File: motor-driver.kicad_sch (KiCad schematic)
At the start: 20 parts, among them J2 SIGNAL, J3 PWR, J4 RTMI

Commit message: Finish draft routing,
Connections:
- net +3.3V: no longer J2.1 (Pin_1)
- net +5V: now also J2.1 (Pin_1); no longer J2.2 (Pin_2)
- no-connect marks 3 -> 4
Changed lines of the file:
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@@
   (junction (at 64.77 151.13) (diameter 0) (color 0 0 0 0)
   )
-  (junction (at 127 127) (diameter 0) (color 0 0 0 0)
-  )
   (junction (at 142.24 149.86) (diameter 0) (color 0 0 0 0)
   )
@@
   )
   (no_connect (at 157.48 92.71))
+  (no_connect (at 140.97 127))
   (no_connect (at 170.18 100.33))
   (no_connect (at 157.48 118.11))
@@
     (stroke (width 0) (type default))
   )
-  (wire (pts (xy 128.27 127) (xy 127 127))
-    (stroke (width 0) (type default))
-  )
   (wire (pts (xy 140.97 142.24) (xy 153.67 142.24))
     (stroke (width 0) (type default))
@@
     (stroke (width 0) (type default))
   )
+  (wire (pts (xy 127 129.54) (xy 128.27 129.54))
+    (stroke (width 0) (type default))
+  )
   (wire (pts (xy 116.84 143.51) (xy 107.95 143.51))
     (stroke (width 0) (type default))
@@
     (stroke (width 0) (type default))
   )
-  (wire (pts (xy 140.97 127) (xy 142.24 127))
-    (stroke (width 0) (type default))
-  )
   (wire (pts (xy 20.32 55.88) (xy 33.02 55.88))
     (stroke (width 0) (type default))
@@
     (stroke (width 0) (type default))
   )
-  (wire (pts (xy 127 129.54) (xy 127 127))
-    (stroke (width 0) (type default))
-  )
   (wire (pts (xy 77.47 73.66) (xy 93.98 73.66))
     (stroke (width 0) (type default))
   )
-  (wire (pts (xy 128.27 129.54) (xy 127 129.54))
-    (stroke (width 0) (type default))
-  )
   (wire (pts (xy 77.47 55.88) (xy 90.17 55.88))
     (stroke (width 0) (type default))
@@
     (stroke (width 0) (type default))
   )
+  (wire (pts (xy 127 127) (xy 128.27 127))
+    (stroke (width 0) (type default))
+  )
   (wire (pts (xy 165.1 147.32) (xy 176.53 147.32))
     (stroke (width 0) (type default))
@@
     (stroke (width 0) (type default))
   )
-  (wire (pts (xy 127 125.73) (xy 127 127))
-    (stroke (width 0) (type default))
-  )
   (wire (pts (xy 20.32 22.86) (xy 33.02 22.86))
     (stroke (width 0) (type default))
@@
   )
   (wire (pts (xy 118.11 151.13) (xy 107.95 151.13))
-    (stroke (width 0) (type default))
-  )
-  (wire (pts (xy 142.24 127) (xy 142.24 125.73))
     (stroke (width 0) (type default))
   )
@@
     )
   )
+  (symbol (lib_id "power:+5V") (at 127 127 90) (unit 1)
+    (in_bom yes) (on_board yes) (dnp no)
+    (property "Reference" "#PWR04" (at 130.81 127 0)
+      (effects (font (size 1.27 1.27)) hide)
+    )
+    (property "Value" "+5V" (at 124.46 127 90)
+      (effects (font (size 1.27 1.27)) (justify left))
+    )
+    (property "Footprint" "" (at 127 127 0)
+      (effects (font (size 1.27 1.27)) hide)
+    )
+    (property "Datasheet" "" (at 127 127 0)
+      (effects (font (size 1.27 1.27)) hide)
+    )
+    (pin "1")
+    (instances
+      (project "motor-driver"
+        (path "/314549f2-cc46-4559-991a-ae9411f3d209/25794513-4b05-4cf2-b97c-a9dcfa280e83"
+          (reference "#PWR04") (unit 1)
+        )
+        (path "/314549f2-cc46-4559-991a-ae9411f3d209"
+          (reference "#PWR069") (unit 1)
+        )
+      )
+    )
+  )
   (symbol (lib_id "Device:R_Small_US") (at 105.41 132.08 90) (unit 1)
     (in_bom yes) (on_board yes) (dnp no)
@@
         (path "/314549f2-cc46-4559-991a-ae9411f3d209"
           (reference "C41") (unit 1)
-        )
-      )
-    )
-  )
-  (symbol (lib_id "power:+3.3V") (at 127 125.73 0) (unit 1)
-    (in_bom yes) (on_board yes) (dnp no)
-    (property "Reference" "#PWR054" (at 127 129.54 0)
-      (effects (font (size 1.27 1.27)) hide)
-    )
-    (property "Value" "+3.3V" (at 124.46 121.92 0)
-      (effects (font (size 1.27 1.27)) (justify left))
-    )
-    (property "Footprint" "" (at 127 125.73 0)
-      (effects (font (size 1.27 1.27)) hide)
-    )
-    (property "Datasheet" "" (at 127 125.73 0)
-      (effects (font (size 1.27 1.27)) hide)
-    )
-    (pin "1")
-    (instances
-      (project "motor-driver"
-        (path "/314549f2-cc46-4559-991a-ae9411f3d209/25794513-4b05-4cf2-b97c-a9dcfa280e83"
-          (reference "#PWR054") (unit 1)
-        )
-        (path "/314549f2-cc46-4559-991a-ae9411f3d209"
-          (reference "#PWR071") (unit 1)
         )
       )
@@
     )
   )
-  (symbol (lib_id "power:+5V") (at 142.24 125.73 0) (unit 1)
-    (in_bom yes) (on_board yes) (dnp no)
-    (property "Reference" "#PWR04" (at 142.24 129.54 0)
-      (effects (font (size 1.27 1.27)) hide)
-    )
-    (property "Value" "+5V" (at 139.7 121.92 0)
-      (effects (font (size 1.27 1.27)) (justify left))
-    )
-    (property "Footprint" "" (at 142.24 125.73 0)
-      (effects (font (size 1.27 1.27)) hide)
-    )
-    (property "Datasheet" "" (at 142.24 125.73 0)
-      (effects (font (size 1.27 1.27)) hide)
-    )
-    (pin "1")
-    (instances
-      (project "motor-driver"
-        (path "/314549f2-cc46-4559-991a-ae9411f3d209/25794513-4b05-4cf2-b97c-a9dcfa280e83"
-          (reference "#PWR04") (unit 1)
-        )
-        (path "/314549f2-cc46-4559-991a-ae9411f3d209"
-          (reference "#PWR069") (unit 1)
-        )
-      )
-    )
-  )
   (symbol (lib_id "power:+24V") (at 175.26 127 90) (unit 1)
     (in_bom yes) (on_board yes) (dnp no)
@@
         )
       )
+    )
+  )
+  (symbol (lib_id "power:+3.3V") (at 127 129.54 90) (unit 1)
+    (in_bom yes) (on_board yes) (dnp no)
+    (property "Reference" "#PWR054" (at 130.81 129.54 0)
+      (effects (font (size 1.27 1.27)) hide)
+    )
+    (property "Value" "+3.3V" (at 124.46 129.54 90)
+      (effects (font (size 1.27 1.27)) (justify left))
+    )
+    (property "Footprint" "" (at 127 129.54 0)
+      (effects (font (size 1.27 1.27)) hide)
+    )
+    (property "Datasheet" "" (at 127 129.54 0)
+      (effects (font (size 1.27 1.27)) hide)
+    )
+    (pin "1")
+    (instances
+      (project "motor-driver"
+        (path "/314549f2-cc46-4559-991a-ae9411f3d209/25794513-4b05-4cf2-b97c-a9dcfa280e83"
+          (reference "#PWR054") (unit 1)
+        )
+        (path "/314549f2-cc46-4559-991a-ae9411f3d209"
+          (reference "#PWR071") (unit 1)
+        )
+      )

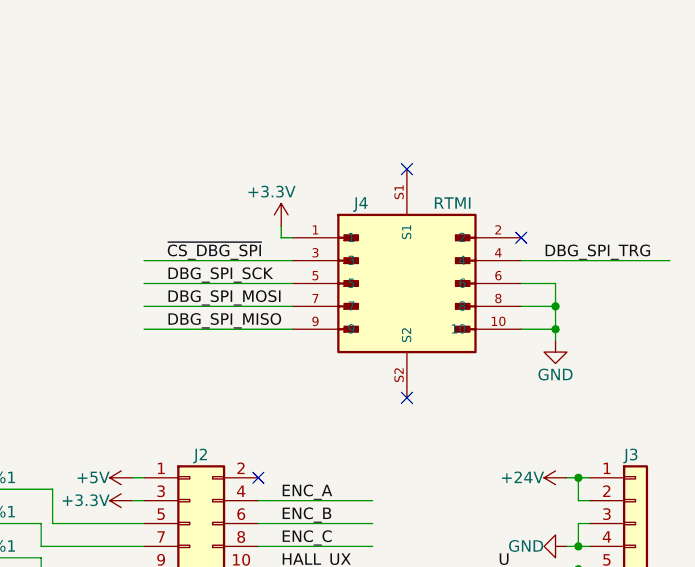
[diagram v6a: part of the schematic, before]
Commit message: Cleanup part properties.
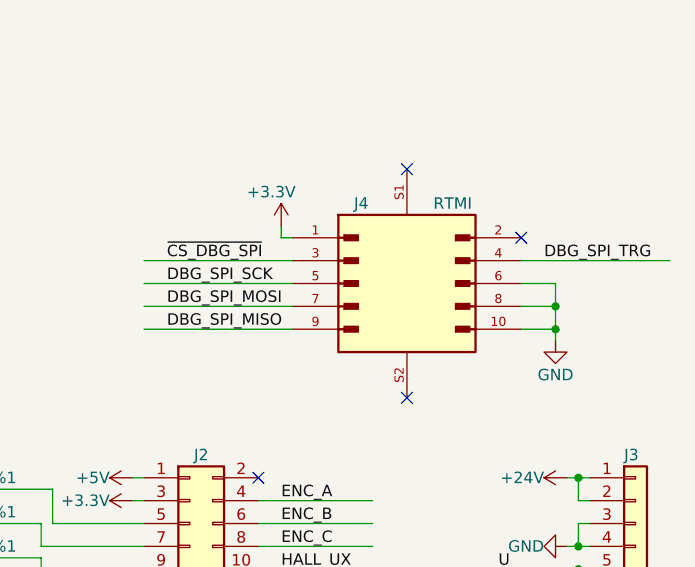
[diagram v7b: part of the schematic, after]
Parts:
- J4: MANUFACTURER Hirose -> (none); MAXIMUM_PACKAGE_HEIGHT 4.8 mm -> (none); PARTREV 20200508 -> (none); STANDARD Manufacturer Recommendations -> (none)
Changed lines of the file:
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@@
       (effects (font (size 1.27 1.27)) hide)
-    )
-    (property "STANDARD" "Manufacturer Recommendations" (at 157.48 105.41 0)
-      (effects (font (size 1.27 1.27)) (justify bottom) hide)
-    )
-    (property "MAXIMUM_PACKAGE_HEIGHT" "4.8 mm" (at 157.48 105.41 0)
-      (effects (font (size 1.27 1.27)) (justify bottom) hide)
-    )
-    (property "MANUFACTURER" "Hirose" (at 157.48 105.41 0)
-      (effects (font (size 1.27 1.27)) (justify bottom) hide)
-    )
-    (property "PARTREV" "20200508" (at 157.48 105.41 0)
-      (effects (font (size 1.27 1.27)) (justify bottom) hide)
     )
     (property "MPN" "DF20EF-10DP-1V(52)" (at 157.48 105.41 0)

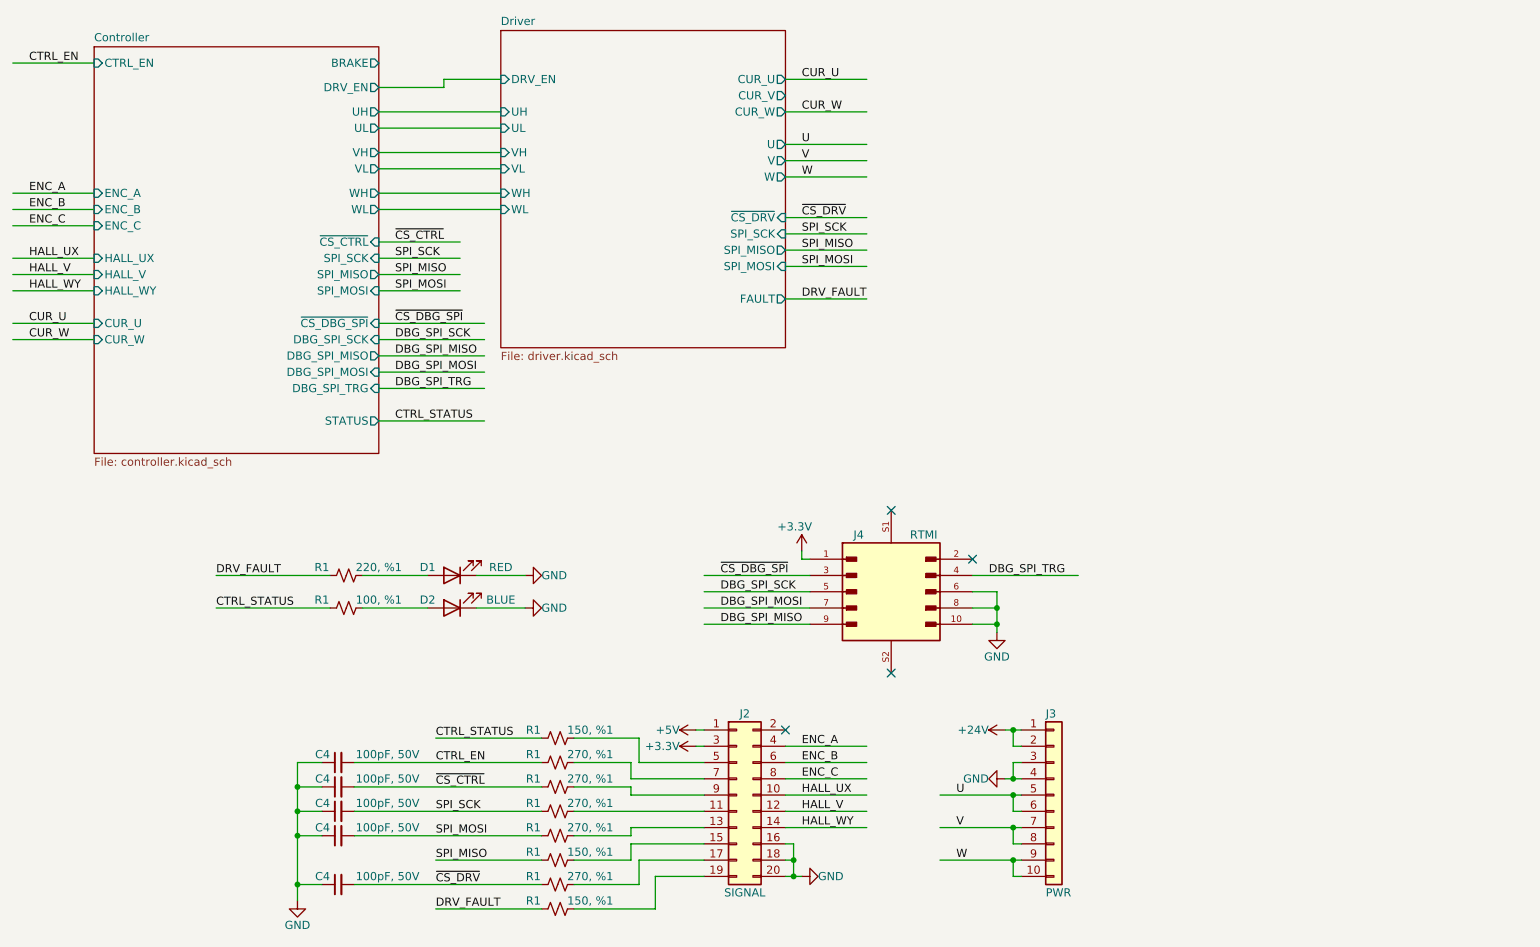
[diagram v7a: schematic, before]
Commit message: Fix issues found during the test, in the schematics.
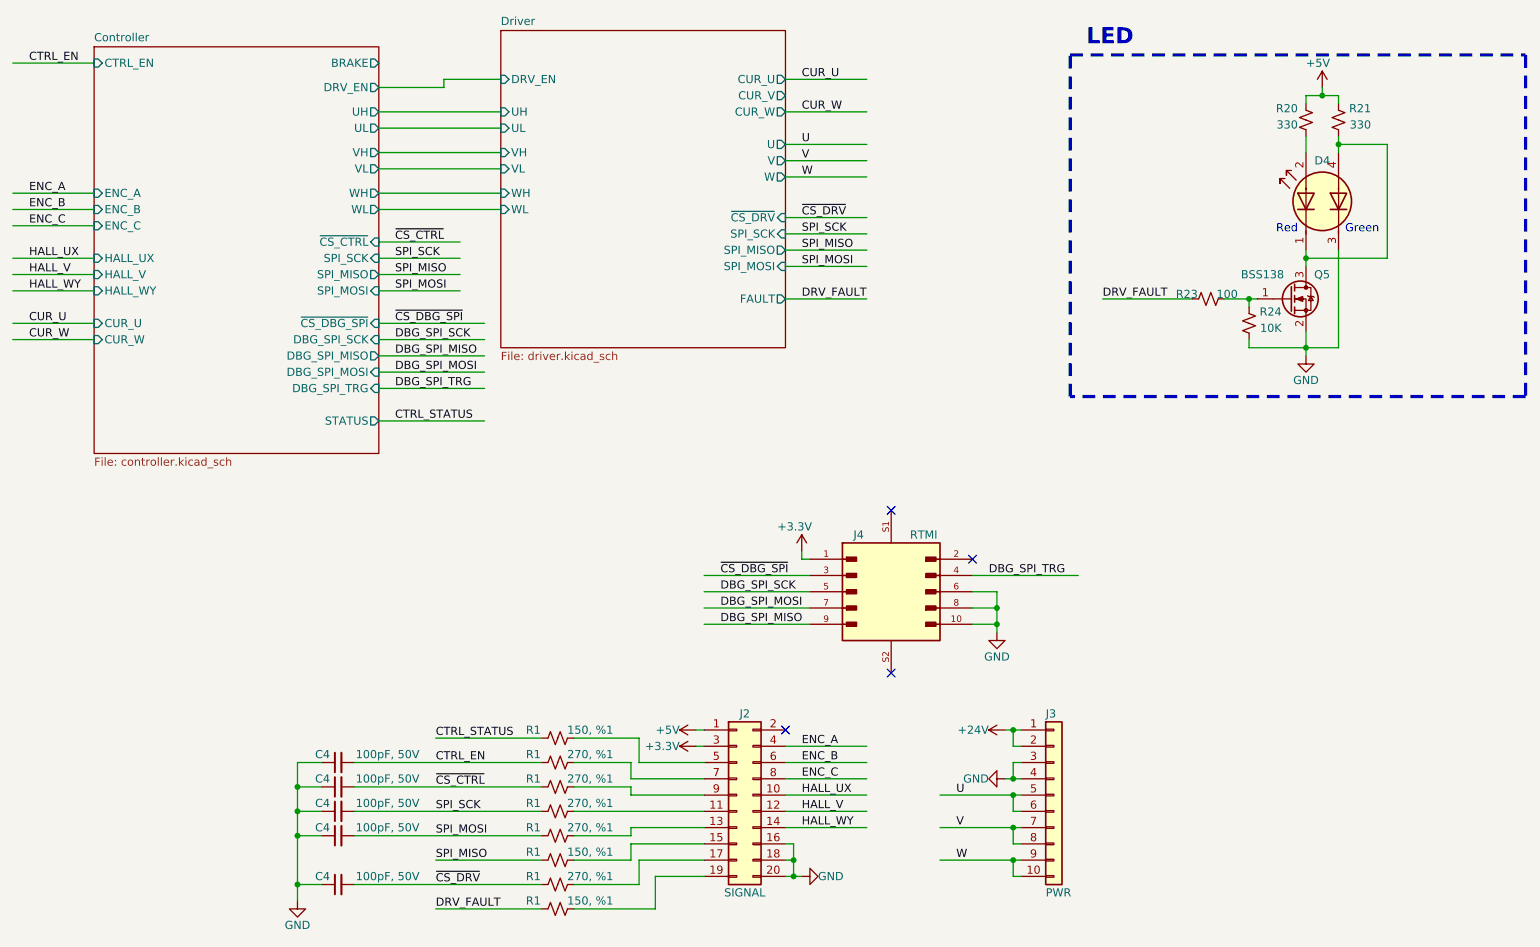
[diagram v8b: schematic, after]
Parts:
- removed D1: RED, LED_SMD:LED_0603_1608Metric, symbol Device:LED
- removed D2: BLUE, LED_SMD:LED_0603_1608Metric, symbol Device:LED
- removed R1: 100, %1, Resistor_SMD:R_0402_1005Metric, symbol Device:R_Small_US
- removed R1: 220, %1, Resistor_SMD:R_0402_1005Metric, symbol Device:R_Small_US
- added D4: LED Dual, LED_SMD:LED_Avago_PLCC4_3.2x2.8mm_CW, symbol Device:LED_Dual_KAKA
- added Q5: BSS138, Package_TO_SOT_SMD:SOT-23, symbol Transistor_FET:BSS138
- added R20, R21: 330, Resistor_SMD:R_0402_1005Metric, symbol Device:R_Small_US
- added R23: 100, Resistor_SMD:R_0402_1005Metric, symbol Device:R_Small_US
- added R24: 10K, Resistor_SMD:R_0402_1005Metric, symbol Device:R_Small_US
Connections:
- net +5V: now also R20.2, R21.2
- net DRV_FAULT: now also R23.2
- net GND: now also D4.3 (A2), Q5.2 (S), R24.1
- new net: Q5.1 (G), R23.1, R24.2
- new net: D4.1 (A1), D4.4 (K2), Q5.3 (D), R21.1
- new net: D4.2 (K1), R20.1
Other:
- note added: "Green"
- note added: "LED"
- note added: "Red"
